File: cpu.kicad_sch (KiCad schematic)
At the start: 6 parts, among them J3 FTSH-105-01-L-DV-K, J4 TS-103-G-A

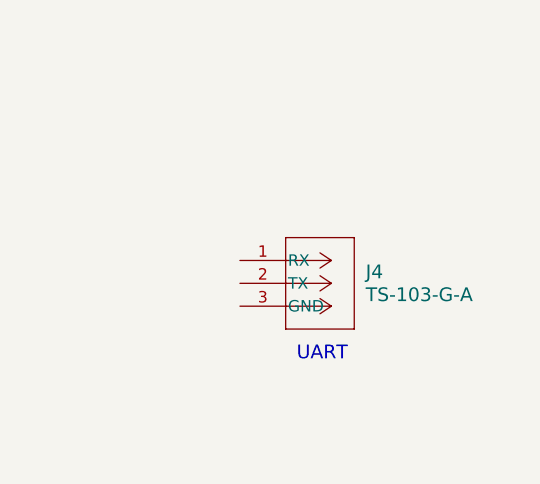
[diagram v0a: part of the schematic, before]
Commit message: Change the connector, power cleanups
Change the PC104 connector. The CSKB specifies ESQ-126-39-G-D, which
have 12.19mm pins.  This leaves around 3mm of pin exposed between the
boards.  This design has ESQ-126-38-G-D PC104 which will leave no space.

Rework the power to a fairly common setup.

Signed-off-by: Corey Minyard <corey@minyard.net>
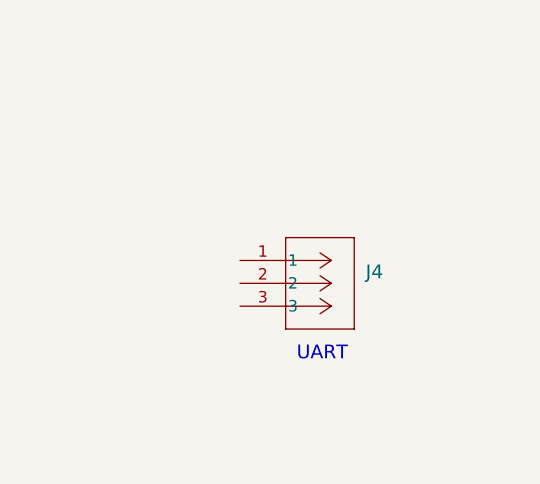
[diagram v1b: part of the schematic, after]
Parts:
- removed J4: TS-103-G-A, Local_Footprints:CON3_1X3_TU_HTS_SAI, symbol Local_Connectors:TS-103-G-A_2-UART
- added J4: TSW-103-08-F-S-RA, Local_Footprints:CON3_1X3_TR_TSW_SAI, symbol PACSAT_DEV_misc:TSW-103-08-F-S-RA
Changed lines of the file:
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@@
-	)
-	(symbol
-		(lib_id "Local_Connectors:TS-103-G-A_2-UART")
-		(at 181.61 91.44 0)
-		(unit 1)
-		(exclude_from_sim no)
-		(in_bom yes)
-		(on_board yes)
-		(dnp no)
-		(fields_autoplaced yes)
-		(property "Reference" "J4"
-			(at 195.58 92.7099 0)
-			(effects
-				(font
-					(size 1.524 1.524)
-				)
-				(justify left)
-			)
-		)
-		(property "Value" "TS-103-G-A"
-			(at 195.58 95.2499 0)
-			(effects
-				(font
-					(size 1.524 1.524)
-				)
-				(justify left)
-			)
-		)
-		(property "Footprint" "Local_Footprints:CON3_1X3_TU_HTS_SAI"
-			(at 181.61 91.44 0)
-			(effects
-				(font
-					(size 1.27 1.27)
-					(italic yes)
-				)
-				(hide yes)
-			)
-		)
-		(property "Datasheet" "TS-103-G-A"
-			(at 181.61 91.44 0)
-			(effects
-				(font
-					(size 1.27 1.27)
-					(italic yes)
-				)
-				(hide yes)
-			)
-		)
-		(property "Description" "1x3 pin UART"
-			(at 181.61 91.44 0)
-			(effects
-				(font
-					(size 1.27 1.27)
-				)
-				(hide yes)
-			)
-		)
-		(pin "1"
-		)
-		(pin "2"
-		)
-		(pin "3"
-		)
-		(instances
-			(project ""
-				(path "/cc9f42d2-6985-41ac-acab-5ab7b01c5b38/adf61ae3-df77-4e04-8bda-b4049a36fcf4"
-					(reference "J4")
-					(unit 1)
-				)
-			)
-		)
 	)
 	(symbol
@@
 					(unit 1)
 				)
+			)
+		)
+	)
+	(symbol
+		(lib_id "PACSAT_DEV_misc:TSW-103-08-F-S-RA")
+		(at 181.61 91.44 0)
+		(unit 1)
+		(exclude_from_sim no)
+		(in_bom yes)
+		(on_board yes)
+		(dnp no)
+		(fields_autoplaced yes)
+		(property "Reference" "J4"
+			(at 195.58 92.7099 0)
+			(effects
+				(font
+					(size 1.524 1.524)
+				)
+				(justify left)
+			)
+		)
+		(property "Value" "TSW-103-08-F-S-RA"
+			(at 195.58 95.2499 0)
+			(effects
+				(font
+					(size 1.524 1.524)
+				)
+				(justify left)
+				(hide yes)
+			)
+		)
+		(property "Footprint" "Local_Footprints:CON3_1X3_TR_TSW_SAI"
+			(at 181.61 91.44 0)
+			(effects
+				(font
+					(size 1.27 1.27)
+					(italic yes)
+				)
+				(hide yes)
+			)
+		)
+		(property "Datasheet" "TSW-103-08-F-S-RA"
+			(at 181.61 91.44 0)
+			(effects
+				(font
+					(size 1.27 1.27)
+					(italic yes)
+				)
+				(hide yes)
+			)
+		)
+		(property "Description" "1x3 pin UART"
+			(at 181.61 91.44 0)
+			(effects
+				(font
+					(size 1.27 1.27)
+				)
+				(hide yes)
+			)
+		)
+		(pin "3"
+		)
+		(pin "2"
+		)
+		(pin "1"
+		)
+		(instances
+			(project "PacSatBaseBoard"
+				(path "/cc9f42d2-6985-41ac-acab-5ab7b01c5b38/adf61ae3-df77-4e04-8bda-b4049a36fcf4"
+					(reference "J4")
+					(unit 1)
+				)
